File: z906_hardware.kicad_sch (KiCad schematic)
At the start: 89 parts, among them J1 USB_C_Receptacle_USB2.0_16P, J5 Ampli, J6 Console, U1 ESP32-S3-WROOM-1, U2 TPS62A02APDDC, U3 PCM5102A, U4 TPD2EUSB30, U6 TPS7A4533DCQ, U7 PCM1860DBT

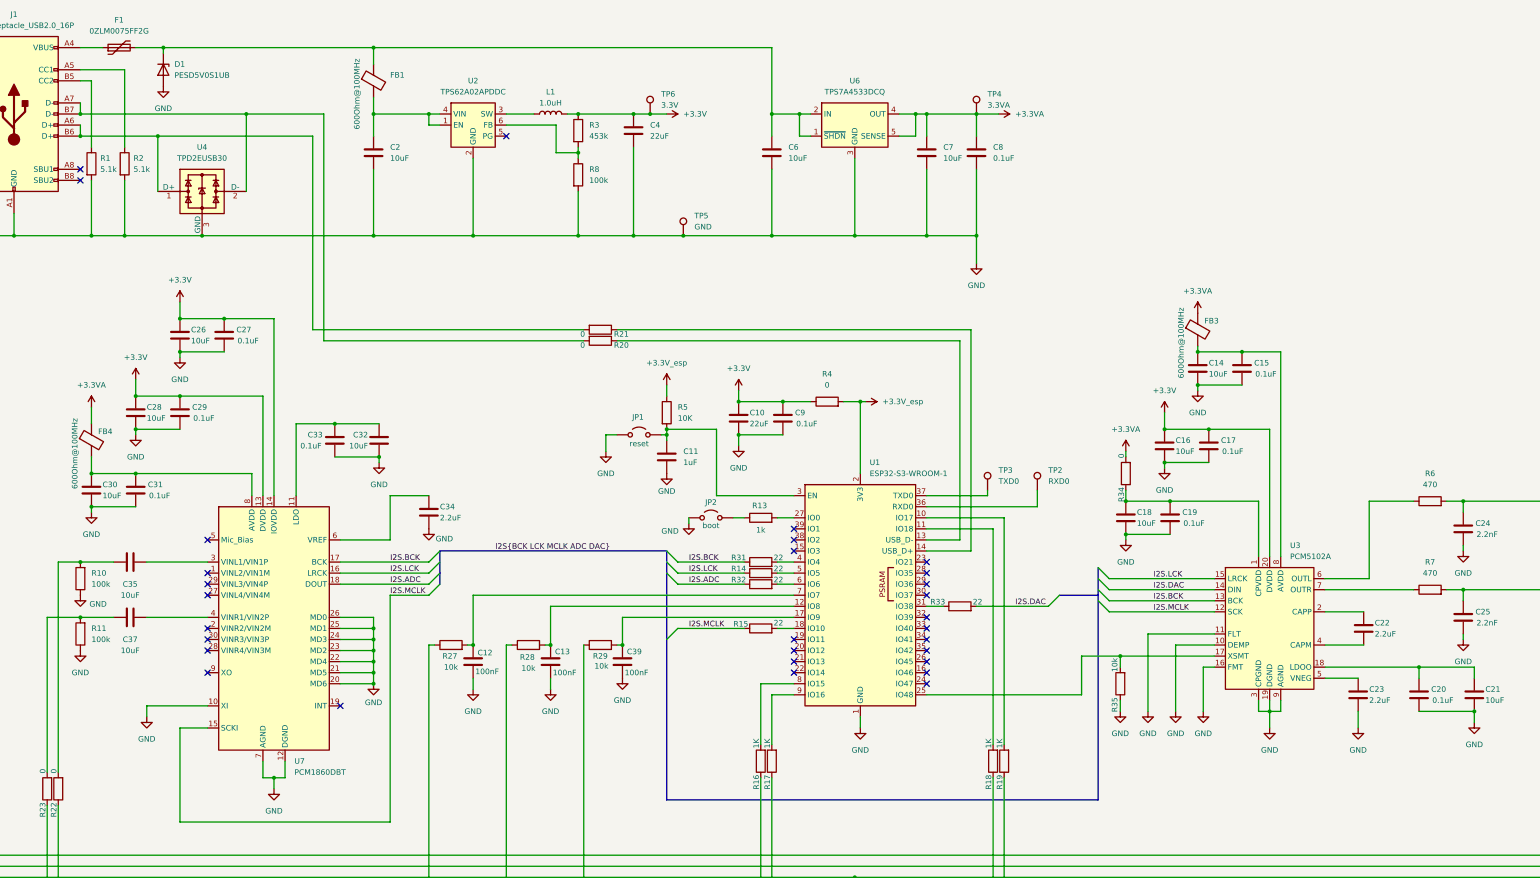
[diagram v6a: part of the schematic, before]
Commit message: start placing composants
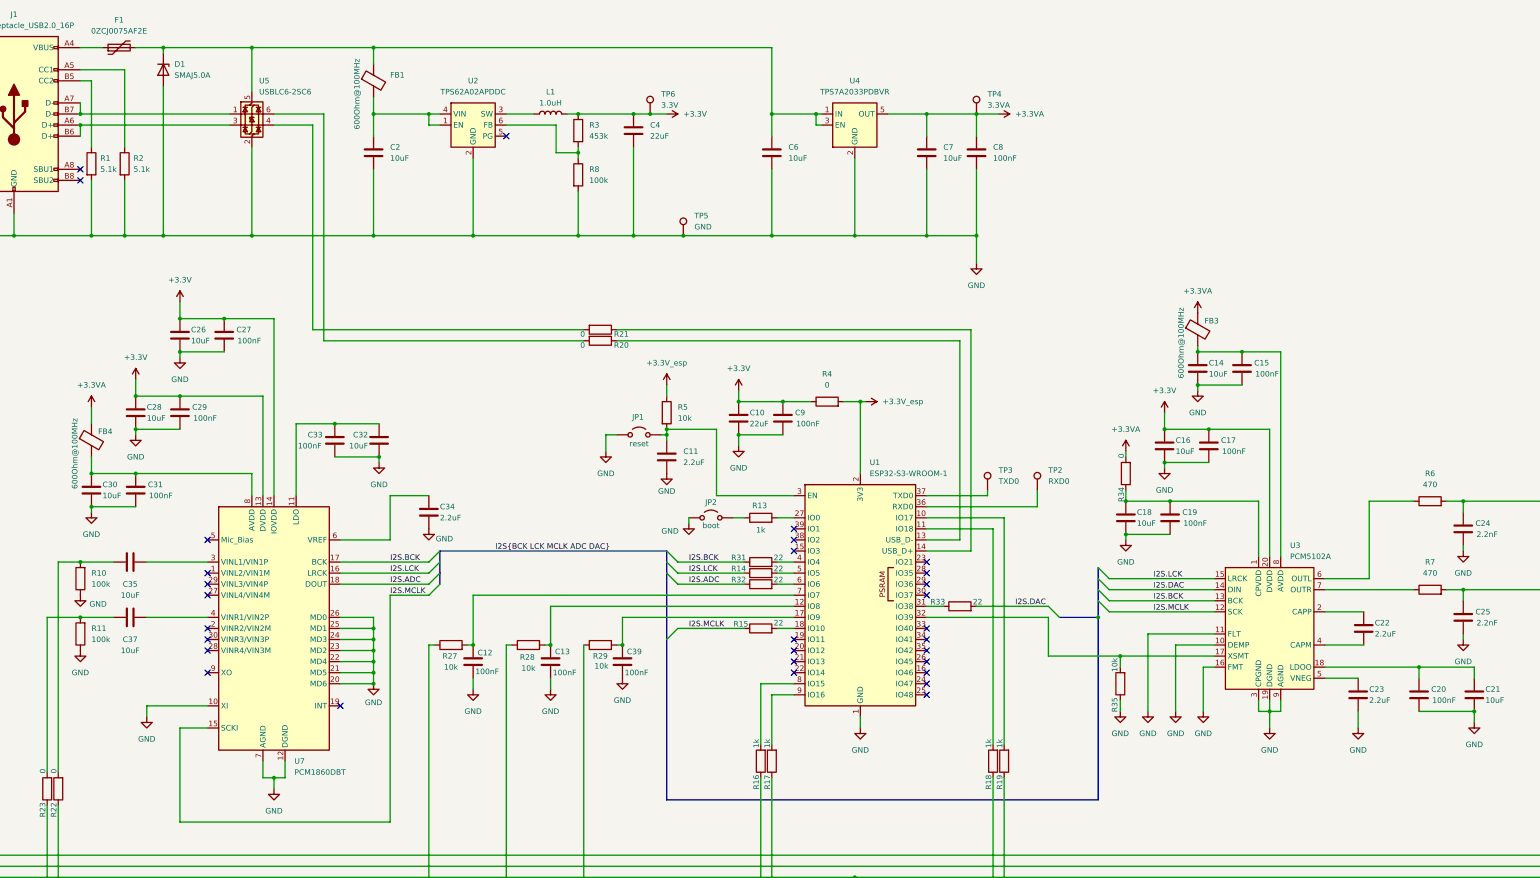
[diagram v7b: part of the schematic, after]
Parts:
- removed U4: TPD2EUSB30, Package_TO_SOT_SMD:Texas_DRT-3, symbol Power_Protection:TPD2EUSB30
- removed U6: TPS7A4533DCQ, Package_TO_SOT_SMD:SOT-223-6_TabPin3, symbol Regulator_Linear:TPS7A45xxKTT
- added U4: TPS7A2033PDBVR, Package_TO_SOT_SMD:SOT-23-5, symbol Regulator_Linear:TPS7A20xxxDBV
- added U5: USBLC6-2SC6, Package_TO_SOT_SMD:SOT-23-6, symbol Power_Protection:USBLC6-2SC6
- C11: value 1uF -> 2.2uF
- C15, C17, C19, C20, C27, C29, C31, C33, C8, C9: value 0.1uF -> 100nF
- D1: value PESD5V0S1UB -> SMAJ5.0A; footprint Diode_SMD:D_SOD-523 -> Diode_SMD:D_SMA
- F1: value 0ZLM0075FF2G -> 0ZCJ0075AF2E; footprint Fuse:Fuse_0603_1608Metric_Pad1.05x0.95mm_HandSolder -> Fuse:Fuse_1210_3225Metric
- J1: footprint Connector_USB:USB_C_Receptacle_HCTL_HC-TYPE-C-16P-01A -> Connector_USB:USB_C_Receptacle_GCT_USB4105-xx-A_16P_TopMnt_Horizontal
- R16, R17, R18, R19: value 1K -> 1k
- R5: value 10K -> 10k
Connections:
- net +3.3VA: now also U4.5 (OUT)
- net GND: now also U4.2 (GND), U5.2 (GND)
- net at J1.A6 (D+), J1.B6 (D+): now also U5.3 (I/O2); no longer R21.2
- net at J1.A7 (D-), J1.B7 (D-): now also U5.1 (I/O1); no longer R20.2
- net at C6.1, D1.1 (K), F1.2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: now also U4.1 (IN), U4.3 (EN), U5.5 (VBUS)
- net at R35.2, U3.17 (XSMT): now also U1.32 (IO39); no longer U1.25 (IO48)
- new net: R20.2, U5.6 (I/O1)
- new net: R21.2, U5.4 (I/O2)
